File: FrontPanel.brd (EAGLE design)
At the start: 45 x 18.5 mm, 11 parts

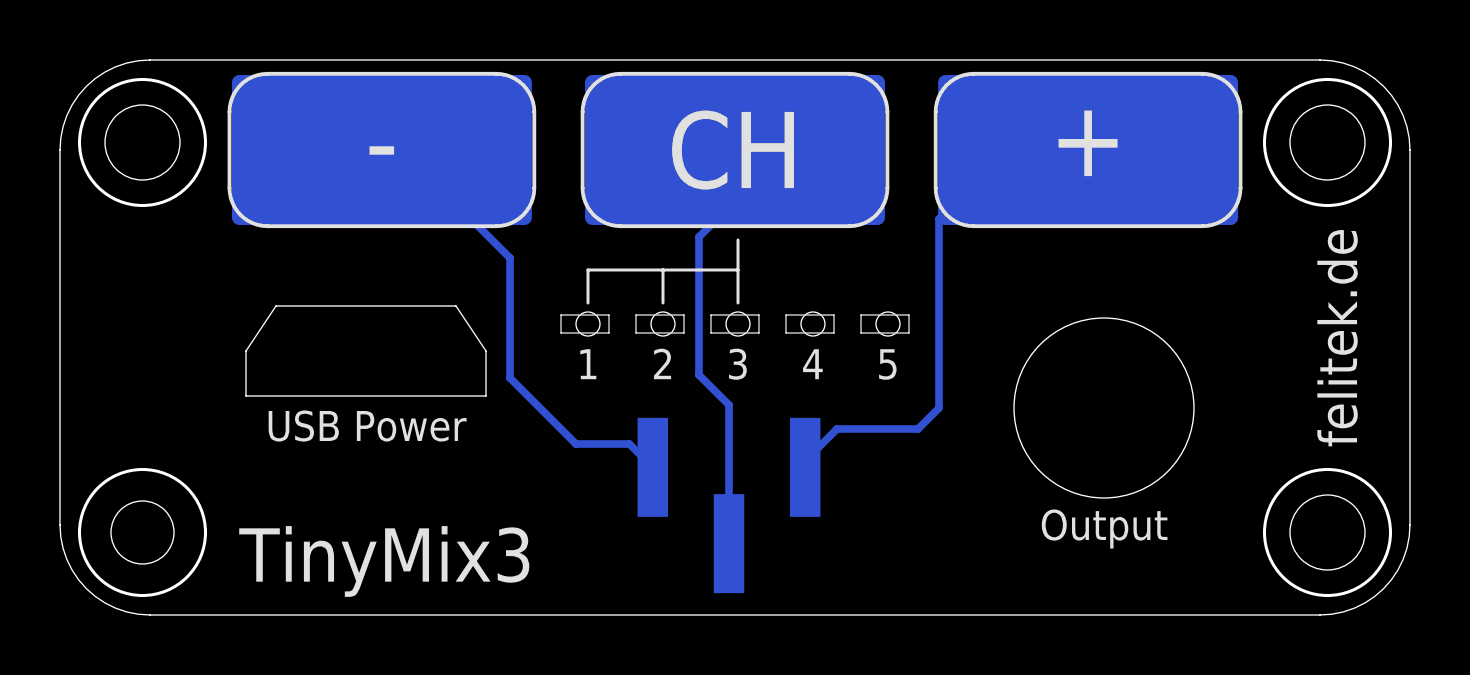
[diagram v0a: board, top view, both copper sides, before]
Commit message: Refactored whole board because due to case layout constraint, the regular through-hole film capacitors couldn't be used anymore. We're now using 1206 SMD film capacitors.
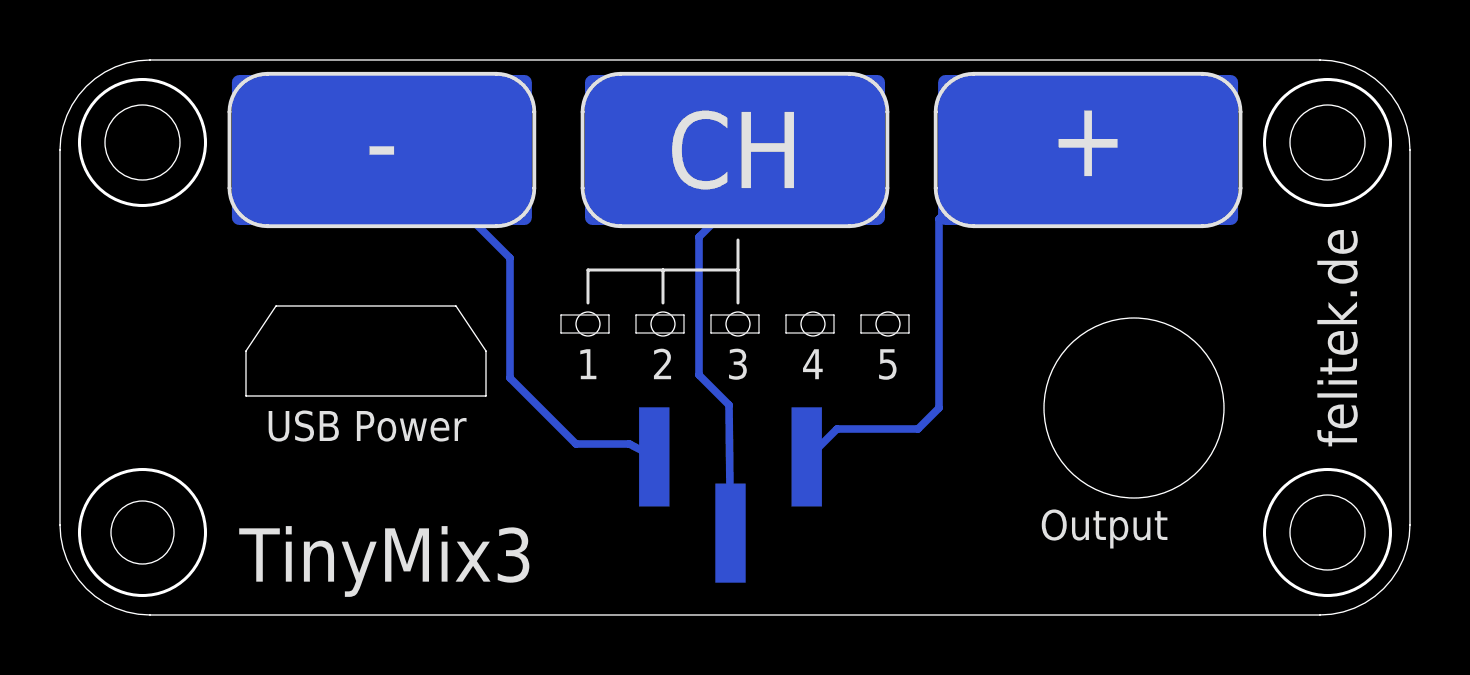
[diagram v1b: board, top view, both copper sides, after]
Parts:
- moved U$1 1.00 mm to (35.8, 6.90)
- moved JP1 0.35 mm to (22.4, 4.00)
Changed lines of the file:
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@@
 <setting verticaltext="up"/>
 </settings>
-<grid distance="0.05" unitdist="inch" unit="inch" style="lines" multiple="1" display="no" altdistance="0.05" altunitdist="mm" altunit="mm"/>
+<grid distance="1" unitdist="mm" unit="mm" style="lines" multiple="1" display="no" altdistance="0.5" altunitdist="mm" altunit="mm"/>
 <layers>
 <layer number="1" name="Top" color="4" fill="1" visible="yes" active="yes"/>
@@
 </autorouter>
 <elements>
-<element name="JP1" library="pinhead" package="1X03SMD" value="" x="22.3" y="3.65" rot="MR0"/>
-<element name="U$1" library="TinyMix3-FrontPanel" package="FC68125-FP" value="" x="34.8" y="6.9"/>
+<element name="JP1" library="pinhead" package="1X03SMD" value="" x="22.35" y="4" rot="MR0">
+<attribute name="PRICE_100" value="0.55510" x="22.35" y="4" size="1.778" layer="28" rot="MR0" display="off"/>
+<attribute name="OC_DIGIKEY" value="S5595-ND" x="22.35" y="4" size="1.778" layer="28" rot="MR0" display="off"/>
+</element>
+<element name="U$1" library="TinyMix3-FrontPanel" package="FC68125-FP" value="" x="35.8" y="6.9"/>
 <element name="U$2" library="TinyMix3-FrontPanel" package="SMDLED_RIGHTANGLE0602" value="" x="27.5" y="9.7" rot="R180"/>
 <element name="U$3" library="TinyMix3-FrontPanel" package="SMDLED_RIGHTANGLE0602" value="" x="25" y="9.7" rot="R180"/>
@@
 <contactref element="JP1" pad="1"/>
 <contactref element="U$8" pad="P$1"/>
-<wire x1="24.84" y1="4.92" x2="24.84" y2="5.14" width="0.254" layer="16"/>
+<wire x1="24.89" y1="5.27" x2="24.84" y2="5.14" width="0.254" layer="16"/>
 <wire x1="24.84" y1="5.14" x2="25.9" y2="6.2" width="0.254" layer="16"/>
 <wire x1="25.9" y1="6.2" x2="28.6" y2="6.2" width="0.254" layer="16"/>
@@
 <contactref element="JP1" pad="2"/>
 <contactref element="U$9" pad="P$1"/>
-<wire x1="22.3" y1="2.38" x2="22.3" y2="7" width="0.254" layer="16"/>
+<wire x1="22.35" y1="2.73" x2="22.3" y2="7" width="0.254" layer="16"/>
 <wire x1="22.3" y1="7" x2="21.3" y2="8" width="0.254" layer="16"/>
 <wire x1="21.3" y1="8" x2="21.3" y2="12.6" width="0.254" layer="16"/>
@@
 <wire x1="15" y1="7.9" x2="17.2" y2="5.7" width="0.254" layer="16"/>
 <wire x1="17.2" y1="5.7" x2="18.98" y2="5.7" width="0.254" layer="16"/>
-<wire x1="18.98" y1="5.7" x2="19.76" y2="4.92" width="0.254" layer="16"/>
+<wire x1="18.98" y1="5.7" x2="19.81" y2="5.27" width="0.254" layer="16"/>
 </signal>
 </signals>
